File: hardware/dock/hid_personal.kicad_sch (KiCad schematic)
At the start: 0 parts

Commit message: Dock schematic: review fixes, Pico 2/XIAO socket+pogo mounting
- Cross HID UART TX/RX; split ROLE_STRAP per endpoint
- VBUS sense (GP4) and USB-C CC current sensing (GP26/27) on HID endpoints
- Pogo +5V via TPS2552 enabled by DET, TPD4E1U06 ESD + 1k on pogo lines
- 2x100uF bulk on SYS_5V and keyboard VBUS; 100k EN pull-down
- Remove TPS62162 rail: XIAO from 5V, pull-ups on module 3V3 rails
- Socketed Pico 2 / XIAO footprints with P50-B1 probe holes for USB+SWD
- XIAO SWD header J8; RP2350 reset control of HID/BLE endpoints
- DESIGN.md: UART allocation, power budget, mounting, reset control
- Add .gitignore, custom libraries and datasheets

Co-Authored-By: Claude Opus 5.5 <noreply@anthropic.com>
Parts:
- added A2: RaspberryPi_Pico, dock:RaspberryPi_Pico2_Socket_Pogo, symbol MCU_Module:RaspberryPi_Pico_Extensive
- added C2: 100nF, Capacitor_SMD:C_0805_2012Metric_Pad1.18x1.45mm_HandSolder, symbol Device:C
- added J3: Conn_01x05_Pin, Connector_PinHeader_2.54mm:PinHeader_1x05_P2.54mm_Vertical, symbol Connector:Conn_01x05_Pin
- added J4: (no value), dock:KLS L-KLS1-5416-L1-01-R, symbol dock_custom:KLS_L-KLS1-5416-L1-01-R
- added R10: 330, Resistor_SMD:R_0805_2012Metric_Pad1.20x1.40mm_HandSolder, symbol Device:R
- added R11, R12: 5.1k, Resistor_SMD:R_0805_2012Metric_Pad1.20x1.40mm_HandSolder, symbol Device:R
- added R13, R29, R30, R36: 10k, Resistor_SMD:R_0805_2012Metric_Pad1.20x1.40mm_HandSolder, symbol Device:R
- added R19: 22k, Resistor_SMD:R_0805_2012Metric_Pad1.20x1.40mm_HandSolder, symbol Device:R
- added R20: 33k, Resistor_SMD:R_0805_2012Metric_Pad1.20x1.40mm_HandSolder, symbol Device:R
- added R33: 1k, Resistor_SMD:R_0805_2012Metric_Pad1.20x1.40mm_HandSolder, symbol Device:R
- added U5: TPD2EUSB30, Package_TO_SOT_SMD:Texas_DRT-3, symbol Power_Protection:TPD2EUSB30
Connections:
- new net: A2.31 (GPIO26_ADC0), R29.1
- new net: A2.32 (GPIO27_ADC1), R30.1
- new net: A2.4 (GPIO2), R13.2
- new net: A2.6 (GPIO4), R19.2, R20.1
- new net: A2.D1 (SWCLK), J3.1 (Pin_1)
- new net: A2.D3 (SWDIO), J3.2 (Pin_2)
- new net: C2.2, J4.SH (SHIELD), R10.1
- new net CC1: J4.4 (CC1_A5), R11.1, R29.2
- new net CC2: J4.10 (CC2_B5), R12.1, R30.2
- new net GND: A2.13 (GND), A2.18 (GND), A2.23 (GND), A2.28 (GND), A2.3 (GND), A2.33 (AGND), A2.38 (GND), A2.8 (GND), A2.D2 (GND), A2.TP1 (USB_GND), C2.1, J3.3 (Pin_3), J4.1 (GND_A1_B12), J4.12 (GND_B1_A12), R10.2, R11.2, R12.2, R13.1, R20.2, U5.3 (GND)
- new net HID_PERSONAL_RUN_CTRL: R33.1
- new net HID_PERSONAL_RX: A2.1 (GPIO0)
- new net HID_PERSONAL_TX: A2.2 (GPIO1)
- new net PERSONAL_VBUS: J4.11 (VBUS_B4_A9), J4.2 (VBUS_A4_B9), R19.1
- new net PICO_3V3: A2.36 (3V3), J3.5 (Pin_5), R36.1
- new net RUN: A2.30 (RUN), J3.4 (Pin_4), R33.2, R36.2
- new net SYS_5V: A2.39 (VSYS)
- new net USB_PERSONAL_DM: A2.TP2 (USB_DM), J4.5 (DM_B7), J4.7 (DM_A7), U5.2 (D-)
- new net USB_PERSONAL_DP: A2.TP3 (USB_DP), J4.6 (DP_A6), J4.8 (DP_B6), U5.1 (D+)
- no-connect marks 0 -> 28
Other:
- note added: "Role_Strap"

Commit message: Net classes, project lib tables, docs and datasheets; PCB synced
- Rename USB pairs to *_D_P/*_D_N; add Power and USB net classes
- Project-relative fp-lib-table and new sym-lib-table
- Pico values set to "Raspberry Pi Pico 2"; J1 symbol synced with library
- DESIGN.md/README: Pico 2 x3 + XIAO modules, TPS2116, pogo switch/ESD,
  VBUS/CC sensing, SWD pinout, resolved and open items
- Add TPS2552/2553, TPD2EUSB30 and P50 probe datasheets
- PCB updated from schematic (F8)

Co-Authored-By: Claude Opus 5.5 <noreply@anthropic.com>
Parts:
- A2: value RaspberryPi_Pico -> Raspberry Pi Pico 2
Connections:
- net USB_PERSONAL_DM renamed USB_PERSONAL_D_N
- net USB_PERSONAL_DP renamed USB_PERSONAL_D_P

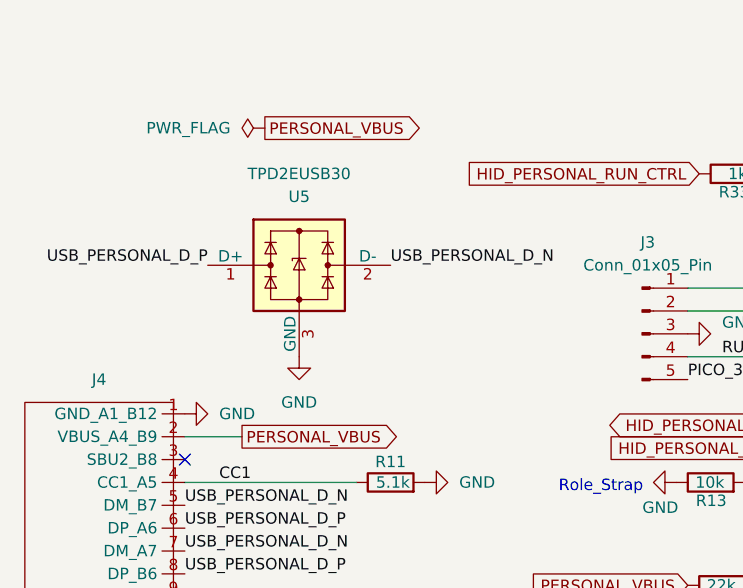
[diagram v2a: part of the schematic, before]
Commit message: USB ESD: TPD2EUSB30 -> TPD4E1U06 on all ports; Pico TP4-6 pads
- U4-U6 now TPD4E1U06 (SOT-23-6, hand-solderable): D+, D-, CC1, CC2
  per port; clamps to GND only, so no back-feed path into PC VBUS
- Keyboard port CC nets named CC1/CC2 (R7/R8 moved along their rows)
- Pico 2 footprint: TP4-TP6 as covered copper-only pads at datasheet
  positions (satisfies F8 pad check, no extra holes)
- Drop unused cached symbols; docs updated; remove TPD2EUSB30 datasheet

Co-Authored-By: Claude Opus 5.5 <noreply@anthropic.com>
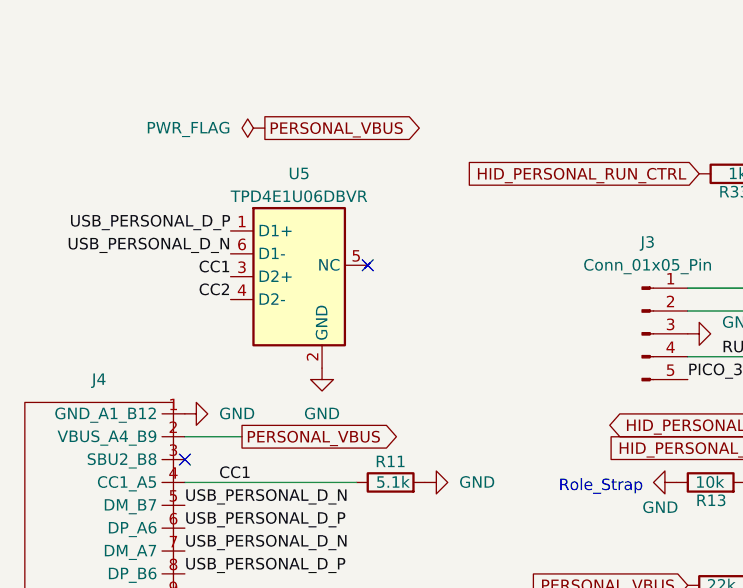
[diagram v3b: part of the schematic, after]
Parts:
- U5: value TPD2EUSB30 -> TPD4E1U06DBVR; footprint Package_TO_SOT_SMD:Texas_DRT-3 -> Package_TO_SOT_SMD:SOT-23-6; symbol Power_Protection:TPD2EUSB30 -> dock_custom:TPD4E1U06DBV
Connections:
- net CC1: now also U5.3 (D2+)
- net CC2: now also U5.4 (D2-)
- net GND: now also U5.2 (GND); no longer U5.3 (GND)
- net USB_PERSONAL_D_N: now also U5.6 (D1-); no longer U5.2 (D-)
- no-connect marks 28 -> 29
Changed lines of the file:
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@@
-		)
-	)
-	(label "USB_PERSONAL_D_P"
-		(at 43.18 66.04 180)
-		(effects
-			(font
-				(size 1.27 1.27)
-			)
-			(justify right bottom)
 		)
 	)
@@
 	(label "RUN"
 		(at 105.41 55.88 0)
-		(effects
-			(font
-				(size 1.27 1.27)
-			)
-			(justify left bottom)
-		)
-	)
-	(label "USB_PERSONAL_D_N"
-		(at 63.5 66.04 0)
 		(effects
 			(font
@@
 	(symbol
 		(lib_id "power:GND")
-		(at 53.34 76.2 0)
-		(unit 1)
-		(body_style 1)
-		(exclude_from_sim no)
-		(in_bom yes)
-		(on_board yes)
-		(in_pos_files yes)
-		(dnp no)
-		(fields_autoplaced yes)
-		(property "Reference" "#PWR027"
-			(at 53.34 82.55 0)
-			(hide yes)
-			(show_name no)
-			(do_not_autoplace no)
-			(effects
-				(font
-					(size 1.27 1.27)
-				)
-			)
-		)
-		(property "Value" "GND"
-			(at 53.34 81.28 0)
-			(show_name no)
-			(do_not_autoplace no)
-			(effects
-				(font
-					(size 1.27 1.27)
-				)
-			)
-		)
-		(property "Footprint" ""
-			(at 53.34 76.2 0)
-			(hide yes)
-			(show_name no)
-			(do_not_autoplace no)
-			(effects
-				(font
-					(size 1.27 1.27)
-				)
-			)
-		)
-		(property "Datasheet" ""
-			(at 53.34 76.2 0)
-			(hide yes)
-			(show_name no)
-			(do_not_autoplace no)
-			(effects
-				(font
-					(size 1.27 1.27)
-				)
-			)
-		)
-		(property "Description" "Power symbol creates a global label with name \"GND\" , ground"
-			(at 53.34 76.2 0)
-			(hide yes)
-			(show_name no)
-			(do_not_autoplace no)
-			(effects
-				(font
-					(size 1.27 1.27)
-				)
-			)
-		)
-		(pin "1"
-		)
-		(instances
-			(project "dock"
-				(path "/b7c42e8e-d530-48de-8d78-684e37659179/1e48719d-5706-44f0-9309-b5d8ee5bd63e"
-					(reference "#PWR027")
-					(unit 1)
-				)
-			)
-		)
-	)
-	(symbol
-		(lib_id "power:GND")
 		(at 95.25 90.17 270)
 		(unit 1)
@@
 				(path "/b7c42e8e-d530-48de-8d78-684e37659179/1e48719d-5706-44f0-9309-b5d8ee5bd63e"
 					(reference "C2")
-					(unit 1)
-				)
-			)
-		)
-	)
-	(symbol
-		(lib_id "Power_Protection:TPD2EUSB30")
-		(at 53.34 66.04 0)
-		(unit 1)
-		(body_style 1)
-		(exclude_from_sim no)
-		(in_bom yes)
-		(on_board yes)
-		(in_pos_files yes)
-		(dnp no)
-		(fields_autoplaced yes)
-		(property "Reference" "U5"
-			(at 53.34 58.42 0)
-			(show_name no)
-			(do_not_autoplace no)
-			(effects
-				(font
-					(size 1.27 1.27)
-				)
-			)
-		)
-		(property "Value" "TPD2EUSB30"
-			(at 53.34 55.88 0)
-			(show_name no)
-			(do_not_autoplace no)
-			(effects
-				(font
-					(size 1.27 1.27)
-				)
-			)
-		)
-		(property "Footprint" "Package_TO_SOT_SMD:Texas_DRT-3"
-			(at 34.29 73.66 0)
-			(hide yes)
-			(show_name no)
-			(do_not_autoplace no)
-			(effects
-				(font
-					(size 1.27 1.27)
-				)
-			)
-		)
-		(property "Datasheet" "http://www.ti.com/lit/ds/symlink/tpd2eusb30a.pdf"
-			(at 53.34 66.04 0)
-			(hide yes)
-			(show_name no)
-			(do_not_autoplace no)
-			(effects
-				(font
-					(size 1.27 1.27)
-				)
-			)
-		)
-		(property "Description" "2-Channel ESD Protection for Super-Speed USB 3.0 Interface, DRT-3"
-			(at 53.34 66.04 0)
-			(hide yes)
-			(show_name no)
-			(do_not_autoplace no)
-			(effects
-				(font
-					(size 1.27 1.27)
-				)
-			)
-		)
-		(pin "1"
-		)
-		(pin "2"
-		)
-		(pin "3"
-		)
-		(instances
-			(project "dock"
-				(path "/b7c42e8e-d530-48de-8d78-684e37659179/1e48719d-5706-44f0-9309-b5d8ee5bd63e"
-					(reference "U5")
 					(unit 1)
 				)
@@
 		)
 	)
+	(symbol
+		(lib_id "dock_custom:TPD4E1U06DBV")
+		(at 53.34 66.04 0)
+		(unit 1)
+		(body_style 1)
+		(exclude_from_sim no)
+		(in_bom yes)
+		(on_board yes)
+		(in_pos_files yes)
+		(dnp no)
+		(property "Reference" "U5"
+			(at 53.34 55.88 0)
+			(show_name no)
+			(do_not_autoplace no)
+			(effects
+				(font
+					(size 1.27 1.27)
+				)
+			)
+		)
+		(property "Value" "TPD4E1U06DBVR"
+			(at 53.34 58.42 0)
+			(show_name no)
+			(do_not_autoplace no)
+			(effects
+				(font
+					(size 1.27 1.27)
+				)
+			)
+		)
+		(property "Footprint" "Package_TO_SOT_SMD:SOT-23-6"
+			(at 53.34 66.04 0)
+			(hide yes)
+			(show_name no)
+			(do_not_autoplace no)
+			(effects
+				(font
+					(size 1.27 1.27)
+				)
+			)
+		)
+		(property "Datasheet" "https://www.ti.com/lit/ds/symlink/tpd4e1u06.pdf"
+			(at 53.34 66.04 0)
+			(hide yes)
+			(show_name no)
+			(do_not_autoplace no)
+			(effects
+				(font
+					(size 1.27 1.27)
+				)
+			)
+		)
+		(property "Description" "Quad-channel unidirectional ESD protection, 5.5V standoff, SOT-23-6"
+			(at 53.34 66.04 0)
+			(hide yes)
+			(show_name no)
+			(do_not_autoplace no)
+			(effects
+				(font
+					(size 1.27 1.27)
+				)
+			)
+		)
+		(pin "1"
+		)
+		(pin "2"
+		)
+		(pin "3"
+		)
+		(pin "4"
+		)
+		(pin "5"
+		)
+		(pin "6"
+		)
+		(instances
+			(project "dock"
+				(path "/b7c42e8e-d530-48de-8d78-684e37659179/1e48719d-5706-44f0-9309-b5d8ee5bd63e"
+					(reference "U5")
+					(unit 1)
+				)
+			)
+		)
+	)
+	(symbol
+		(lib_id "power:GND")
+		(at 55.88 77.47 0)
+		(unit 1)
+		(body_style 1)
+		(exclude_from_sim no)
+		(in_bom yes)
+		(on_board yes)
+		(in_pos_files yes)
+		(dnp no)
+		(fields_autoplaced yes)
+		(property "Reference" "#PWR027"
+			(at 55.88 83.82 0)
+			(hide yes)
+			(show_name no)
+			(do_not_autoplace no)
+			(effects
+				(font
+					(size 1.27 1.27)
+				)
+			)
+		)
+		(property "Value" "GND"
+			(at 55.88 82.55 0)
+			(show_name no)
+			(do_not_autoplace no)
+			(effects
+				(font
+					(size 1.27 1.27)
+				)
+			)
+		)
+		(property "Footprint" ""
+			(at 55.88 77.47 0)
+			(hide yes)
+			(show_name no)
+			(do_not_autoplace no)
+			(effects
+				(font
+					(size 1.27 1.27)
+				)
+			)
+		)
+		(property "Datasheet" ""
+			(at 55.88 77.47 0)
+			(hide yes)
+			(show_name no)
+			(do_not_autoplace no)
+			(effects
+				(font
+					(size 1.27 1.27)
+				)
+			)
+		)
+		(property "Description" "Power symbol creates a global label with name \"GND\" , ground"
+			(at 55.88 77.47 0)
+			(hide yes)
+			(show_name no)
+			(do_not_autoplace no)
+			(effects
+				(font
+					(size 1.27 1.27)
+				)
+			)
+		)
+		(pin "1"
+		)
+		(instances
+			(project "dock"
+				(path "/b7c42e8e-d530-48de-8d78-684e37659179/1e48719d-5706-44f0-9309-b5d8ee5bd63e"
+					(reference "#PWR027")
+					(unit 1)
+				)
+			)
+		)
+	)
+	(no_connect
+		(at 60.96 66.04)
+	)
+	(label "USB_PERSONAL_D_P"
+		(at 45.72 62.23 180)
+		(effects
+			(font
+				(size 1.27 1.27)
+			)
+			(justify right bottom)
+		)
+	)
+	(label "USB_PERSONAL_D_N"
+		(at 45.72 64.77 180)
+		(effects
+			(font
+				(size 1.27 1.27)
+			)
+			(justify right bottom)
+		)
+	)
+	(label "CC1"
+		(at 45.72 67.31 180)
+		(effects
+			(font
+				(size 1.27 1.27)
+			)
+			(justify right bottom)
+		)
+	)
+	(label "CC2"
+		(at 45.72 69.85 180)
+		(effects
+			(font
+				(size 1.27 1.27)
+			)
+			(justify right bottom)
+		)
+	)

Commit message: Set part values; drop unused Seeed library; add Panasonic FK datasheet
- U3 value TPS2553DBVR, J1/J4/J5 value L-KLS1-5416-L1-01-R
- Remove hardware/libraries/seed-xio and its fp-lib-table entry (XIAO now
  uses dock:XIAO_nRF52840_Socket_Pogo; nothing references xiao:)
- Add Panasonic FK series catalog (C13-C16, EEE-FK1E101XP)

Co-Authored-By: Claude Opus 5.5 <noreply@anthropic.com>
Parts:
- J4: value (none) -> L-KLS1-5416-L1-01-R
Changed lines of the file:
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@@
 			)
 		)
-		(property "Value" ""
+		(property "Value" "L-KLS1-5416-L1-01-R"
 			(at 40.64 88.9 0)
 			(show_name no)
